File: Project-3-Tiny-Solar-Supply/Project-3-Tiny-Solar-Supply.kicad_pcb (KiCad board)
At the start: 2 copper layers, 39.7 x 18.5 mm, 16 parts, among them J1 Conn_01x02_Pin, J2 Conn_01x02_Pin, J3 Conn_01x02_Pin, J4 Conn_01x02_Pin, Q1 2N7002, U1 AP3015AKTR-G1

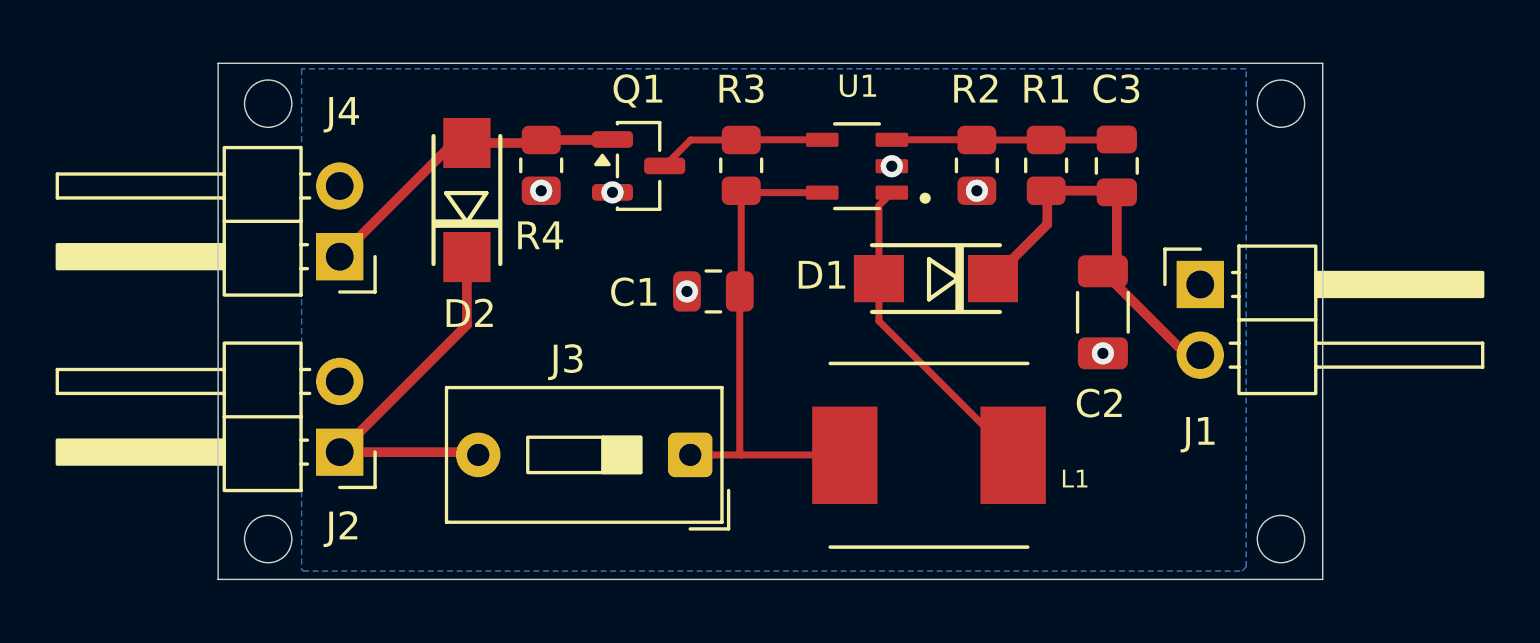
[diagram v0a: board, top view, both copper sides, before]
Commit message: round board's corners, lock drill holes
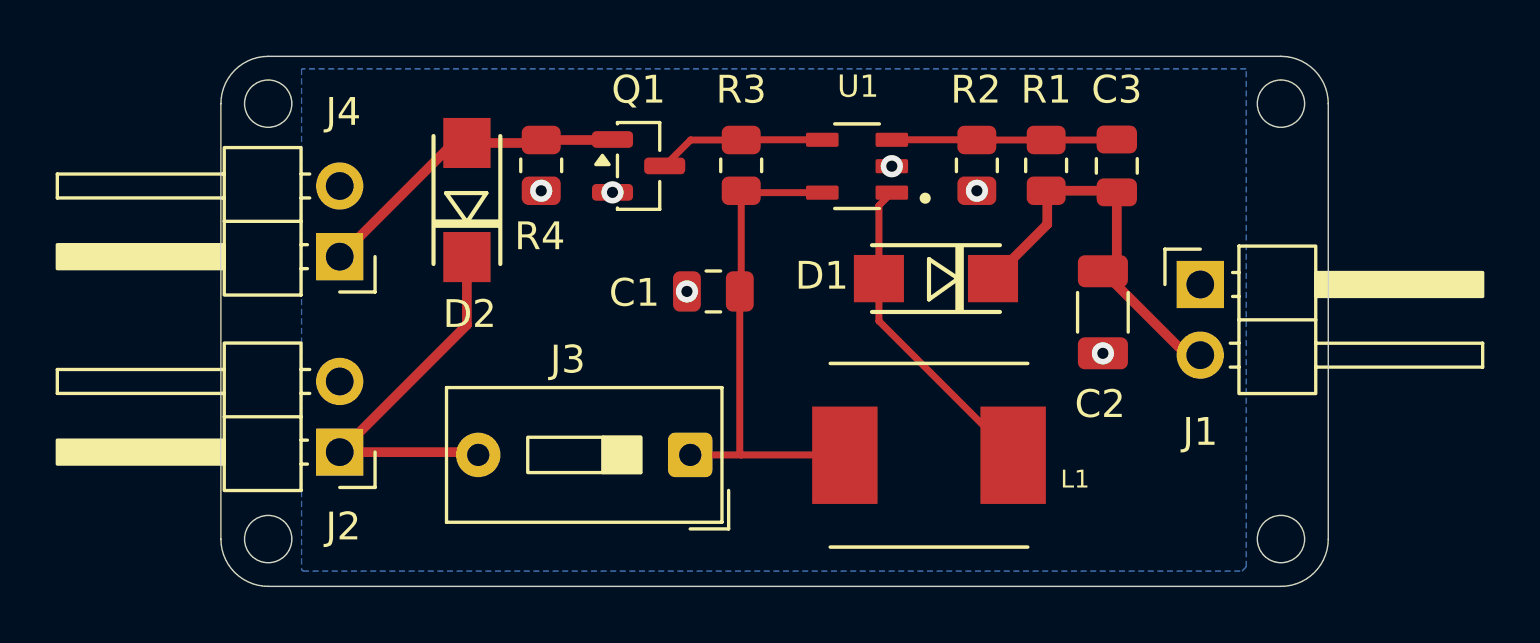
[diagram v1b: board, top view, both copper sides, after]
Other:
- board size 39.7 x 18.5 mm -> 39.8 x 19 mm
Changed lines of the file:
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@@
 		)
 	)
-	(gr_rect
-		(start 38.2 83.55)
-		(end 77.9 102.1)
+	(gr_arc
+		(start 38.3 85)
+		(mid 38.797918 83.797918)
+		(end 40 83.3)
 		(stroke
 			(width 0.05)
 			(type default)
 		)
-		(fill no)
+		(layer "Edge.Cuts")
+	)
+	(gr_line
+		(start 38.3 100.65)
+		(end 38.3 85)
+		(stroke
+			(width 0.05)
+			(type default)
+		)
+		(layer "Edge.Cuts")
+	)
+	(gr_line
+		(start 40 83.3)
+		(end 76.4 83.3)
+		(stroke
+			(width 0.05)
+			(type default)
+		)
 		(layer "Edge.Cuts")
 	)
@@
 		)
 		(fill no)
+		(locked yes)
 		(layer "Edge.Cuts")
 	)
@@
 		)
 		(fill no)
+		(locked yes)
+		(layer "Edge.Cuts")
+	)
+	(gr_arc
+		(start 40 102.35)
+		(mid 38.797918 101.852082)
+		(end 38.3 100.65)
+		(stroke
+			(width 0.05)
+			(type default)
+		)
+		(layer "Edge.Cuts")
+	)
+	(gr_arc
+		(start 76.4 83.3)
+		(mid 77.602082 83.797918)
+		(end 78.1 85)
+		(stroke
+			(width 0.05)
+			(type default)
+		)
 		(layer "Edge.Cuts")
 	)
@@
 		)
 		(fill no)
+		(locked yes)
 		(layer "Edge.Cuts")
 	)
@@
 		)
 		(fill no)
+		(locked yes)
 		(layer "Edge.Cuts")
 	)
+	(gr_line
+		(start 76.4 102.35)
+		(end 40 102.35)
+		(stroke
+			(width 0.05)
+			(type default)
+		)
+		(layer "Edge.Cuts")
+	)
+	(gr_line
+		(start 78.1 85)
+		(end 78.1 100.65)
+		(stroke
+			(width 0.05)
+			(type default)
+		)
+		(layer "Edge.Cuts")
+	)
+	(gr_arc
+		(start 78.1 100.65)
+		(mid 77.602082 101.852082)
+		(end 76.4 102.35)
+		(stroke
+			(width 0.05)
+			(type default)
+		)
+		(layer "Edge.Cuts")
+	)

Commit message: unhatch the back side GNDD plane, add silkscreen logo and text to the back side
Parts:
- added REF**: KiCad-Logo2_5mm_SilkScreen, Symbol:KiCad-Logo2_5mm_SilkScreen, B.Cu at (63.8, 97.8)
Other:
- board text added: "+"
- board text added: "-"
